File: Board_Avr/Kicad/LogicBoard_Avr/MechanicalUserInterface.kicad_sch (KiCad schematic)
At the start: 12 parts, among them J1 I2C_Interface, J2 UART_Interface, J3 Mechanical user interface mai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, U2 TLP291

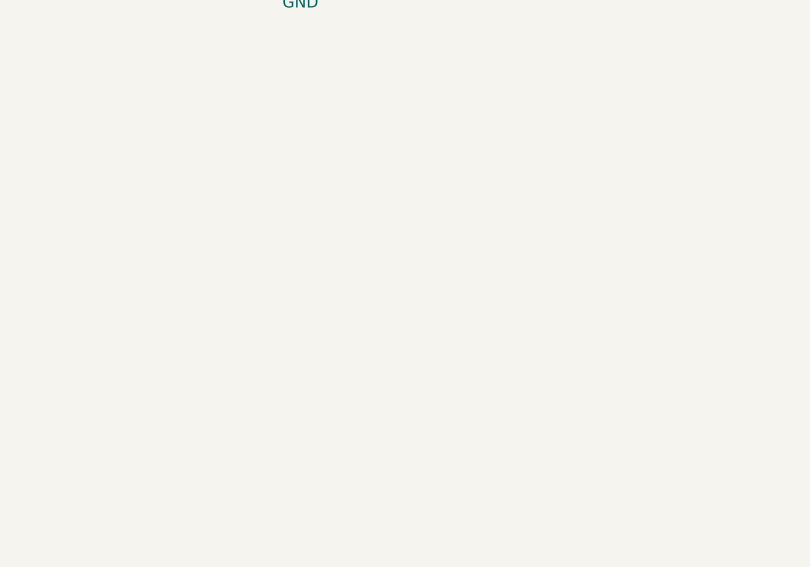
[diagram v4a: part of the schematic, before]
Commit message: Finalised routing and finalised silkscreen
Signed-off-by: bebenlebricolo <benoittarrade@hotmail.fr>
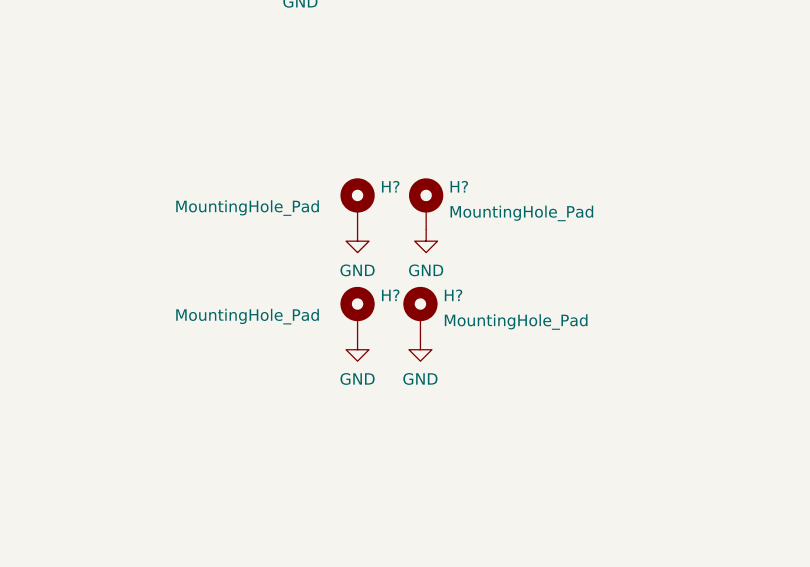
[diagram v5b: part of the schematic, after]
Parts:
- added H? (x4): MountingHole_Pad, MountingHole:MountingHole_2.5mm_Pad_Via, symbol Mechanical:MountingHole_Pad
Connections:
- net GND: now also H?.1, H?.1, H?.1, H?.1
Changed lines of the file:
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@@
     (pin "2")
+  )
+  (symbol (lib_id "power:GND") (at 160.02 139.065 0) (unit 1)
+    (in_bom yes) (on_board yes) (fields_autoplaced)
+    (property "Reference" "#PWR?" (id 0) (at 160.02 145.415 0)
+      (effects (font (size 1.27 1.27)) hide)
+    )
+    (property "Value" "GND" (id 1) (at 160.02 143.6275 0))
+    (property "Footprint" "" (id 2) (at 160.02 139.065 0)
+      (effects (font (size 1.27 1.27)) hide)
+    )
+    (property "Datasheet" "" (id 3) (at 160.02 139.065 0)
+      (effects (font (size 1.27 1.27)) hide)
+    )
+    (pin "1")
   )
   (symbol (lib_id "power:GND") (at 161.925 47.625 90) (unit 1)
@@
     (pin "1")
   )
+  (symbol (lib_id "Mechanical:MountingHole_Pad") (at 160.02 136.525 0) (unit 1)
+    (in_bom yes) (on_board yes) (fields_autoplaced)
+    (property "Reference" "H?" (id 0) (at 162.56 134.3465 0)
+      (effects (font (size 1.27 1.27)) (justify left))
+    )
+    (property "Value" "MountingHole_Pad" (id 1) (at 162.56 137.1216 0)
+      (effects (font (size 1.27 1.27)) (justify left))
+    )
+    (property "Footprint" "MountingHole:MountingHole_2.5mm_Pad_Via" (id 2) (at 160.02 136.525 0)
+      (effects (font (size 1.27 1.27)) hide)
+    )
+    (property "Datasheet" "~" (id 3) (at 160.02 136.525 0)
+      (effects (font (size 1.27 1.27)) hide)
+    )
+    (pin "1")
+  )
+  (symbol (lib_id "Mechanical:MountingHole_Pad") (at 153.035 136.525 0) (unit 1)
+    (in_bom yes) (on_board yes)
+    (property "Reference" "H?" (id 0) (at 155.575 134.3465 0)
+      (effects (font (size 1.27 1.27)) (justify left))
+    )
+    (property "Value" "MountingHole_Pad" (id 1) (at 132.715 136.525 0)
+      (effects (font (size 1.27 1.27)) (justify left))
+    )
+    (property "Footprint" "MountingHole:MountingHole_2.5mm_Pad_Via" (id 2) (at 153.035 136.525 0)
+      (effects (font (size 1.27 1.27)) hide)
+    )
+    (property "Datasheet" "~" (id 3) (at 153.035 136.525 0)
+      (effects (font (size 1.27 1.27)) hide)
+    )
+    (pin "1")
+  )
   (symbol (lib_id "power:GND1") (at 60.325 137.795 0) (unit 1)
     (in_bom yes) (on_board yes)
@@
     (pin "4")
   )
+  (symbol (lib_id "power:GND") (at 160.655 127 0) (unit 1)
+    (in_bom yes) (on_board yes) (fields_autoplaced)
+    (property "Reference" "#PWR?" (id 0) (at 160.655 133.35 0)
+      (effects (font (size 1.27 1.27)) hide)
+    )
+    (property "Value" "GND" (id 1) (at 160.655 131.5625 0))
+    (property "Footprint" "" (id 2) (at 160.655 127 0)
+      (effects (font (size 1.27 1.27)) hide)
+    )
+    (property "Datasheet" "" (id 3) (at 160.655 127 0)
+      (effects (font (size 1.27 1.27)) hide)
+    )
+    (pin "1")
+  )
   (symbol (lib_id "power:GND") (at 161.925 57.785 90) (unit 1)
     (in_bom yes) (on_board yes)
@@
       (effects (font (size 1.27 1.27)) hide)
     )
+    (pin "1")
+  )
+  (symbol (lib_id "Mechanical:MountingHole_Pad") (at 153.035 124.46 0) (unit 1)
+    (in_bom yes) (on_board yes)
+    (property "Reference" "H?" (id 0) (at 155.575 122.2815 0)
+      (effects (font (size 1.27 1.27)) (justify left))
+    )
+    (property "Value" "MountingHole_Pad" (id 1) (at 132.715 124.46 0)
+      (effects (font (size 1.27 1.27)) (justify left))
+    )
+    (property "Footprint" "MountingHole:MountingHole_2.5mm_Pad_Via" (id 2) (at 153.035 124.46 0)
+      (effects (font (size 1.27 1.27)) hide)
+    )
+    (property "Datasheet" "~" (id 3) (at 153.035 124.46 0)
+      (effects (font (size 1.27 1.27)) hide)
+    )
+    (pin "1")
+  )
+  (symbol (lib_id "power:GND") (at 153.035 127 0) (unit 1)
+    (in_bom yes) (on_board yes) (fields_autoplaced)
+    (property "Reference" "#PWR?" (id 0) (at 153.035 133.35 0)
+      (effects (font (size 1.27 1.27)) hide)
+    )
+    (property "Value" "GND" (id 1) (at 153.035 131.5625 0))
+    (property "Footprint" "" (id 2) (at 153.035 127 0)
+      (effects (font (size 1.27 1.27)) hide)
+    )
+    (property "Datasheet" "" (id 3) (at 153.035 127 0)
+      (effects (font (size 1.27 1.27)) hide)
+    )
+    (pin "1")
+  )
+  (symbol (lib_id "Mechanical:MountingHole_Pad") (at 160.655 124.46 0) (unit 1)
+    (in_bom yes) (on_board yes) (fields_autoplaced)
+    (property "Reference" "H?" (id 0) (at 163.195 122.2815 0)
+      (effects (font (size 1.27 1.27)) (justify left))
+    )
+    (property "Value" "MountingHole_Pad" (id 1) (at 163.195 125.0566 0)
+      (effects (font (size 1.27 1.27)) (justify left))
+    )
+    (property "Footprint" "MountingHole:MountingHole_2.5mm_Pad_Via" (id 2) (at 160.655 124.46 0)
+      (effects (font (size 1.27 1.27)) hide)
+    )
+    (property "Datasheet" "~" (id 3) (at 160.655 124.46 0)
+      (effects (font (size 1.27 1.27)) hide)
+    )
+    (pin "1")
+  )
+  (symbol (lib_id "power:GND") (at 153.035 139.065 0) (unit 1)
+    (in_bom yes) (on_board yes) (fields_autoplaced)
+    (property "Reference" "#PWR?" (id 0) (at 153.035 145.415 0)
+      (effects (font (size 1.27 1.27)) hide)
+    )
+    (property "Value" "GND" (id 1) (at 153.035 143.6275 0))
+    (property "Footprint" "" (id 2) (at 153.035 139.065 0)
+      (effects (font (size 1.27 1.27)) hide)
+    )
+    (property "Datasheet" "" (id 3) (at 153.035 139.065 0)
+      (effects (font (size 1.27 1.27)) hide)
+    )

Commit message: Backed up modifications on schematic as well
Signed-off-by: bebenlebricolo <benoittarrade@hotmail.fr>
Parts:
- gave numbers to parts that had none: 4
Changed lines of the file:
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@@
   (symbol (lib_id "power:GND") (at 160.02 139.065 0) (unit 1)
     (in_bom yes) (on_board yes) (fields_autoplaced)
-    (property "Reference" "#PWR?" (id 0) (at 160.02 145.415 0)
+    (property "Reference" "#PWR09" (id 0) (at 160.02 145.415 0)
       (effects (font (size 1.27 1.27)) hide)
     )
@@
   (symbol (lib_id "Mechanical:MountingHole_Pad") (at 160.02 136.525 0) (unit 1)
     (in_bom yes) (on_board yes) (fields_autoplaced)
-    (property "Reference" "H?" (id 0) (at 162.56 134.3465 0)
+    (property "Reference" "H3" (id 0) (at 162.56 134.3465 0)
       (effects (font (size 1.27 1.27)) (justify left))
     )
@@
   (symbol (lib_id "Mechanical:MountingHole_Pad") (at 153.035 136.525 0) (unit 1)
     (in_bom yes) (on_board yes)
-    (property "Reference" "H?" (id 0) (at 155.575 134.3465 0)
+    (property "Reference" "H2" (id 0) (at 155.575 134.3465 0)
       (effects (font (size 1.27 1.27)) (justify left))
     )
@@
   (symbol (lib_id "power:GND") (at 160.655 127 0) (unit 1)
     (in_bom yes) (on_board yes) (fields_autoplaced)
-    (property "Reference" "#PWR?" (id 0) (at 160.655 133.35 0)
+    (property "Reference" "#PWR016" (id 0) (at 160.655 133.35 0)
       (effects (font (size 1.27 1.27)) hide)
     )
@@
   (symbol (lib_id "Mechanical:MountingHole_Pad") (at 153.035 124.46 0) (unit 1)
     (in_bom yes) (on_board yes)
-    (property "Reference" "H?" (id 0) (at 155.575 122.2815 0)
+    (property "Reference" "H1" (id 0) (at 155.575 122.2815 0)
       (effects (font (size 1.27 1.27)) (justify left))
     )
@@
   (symbol (lib_id "power:GND") (at 153.035 127 0) (unit 1)
     (in_bom yes) (on_board yes) (fields_autoplaced)
-    (property "Reference" "#PWR?" (id 0) (at 153.035 133.35 0)
+    (property "Reference" "#PWR06" (id 0) (at 153.035 133.35 0)
       (effects (font (size 1.27 1.27)) hide)
     )
@@
   (symbol (lib_id "Mechanical:MountingHole_Pad") (at 160.655 124.46 0) (unit 1)
     (in_bom yes) (on_board yes) (fields_autoplaced)
-    (property "Reference" "H?" (id 0) (at 163.195 122.2815 0)
+    (property "Reference" "H4" (id 0) (at 163.195 122.2815 0)
       (effects (font (size 1.27 1.27)) (justify left))
     )
@@
   (symbol (lib_id "power:GND") (at 153.035 139.065 0) (unit 1)
     (in_bom yes) (on_board yes) (fields_autoplaced)
-    (property "Reference" "#PWR?" (id 0) (at 153.035 145.415 0)
-      (effects (font (size 1.27 1.27)) hide)
-    )
+    (property "Reference" "#PWR07" (id 0) (at 153.035 145.415 0)
+      (effects (font (size 1.27 1.27)) hide)
+    )
